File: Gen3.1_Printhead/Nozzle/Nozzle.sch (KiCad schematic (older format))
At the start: 74 parts, among them J1 IDC Conn

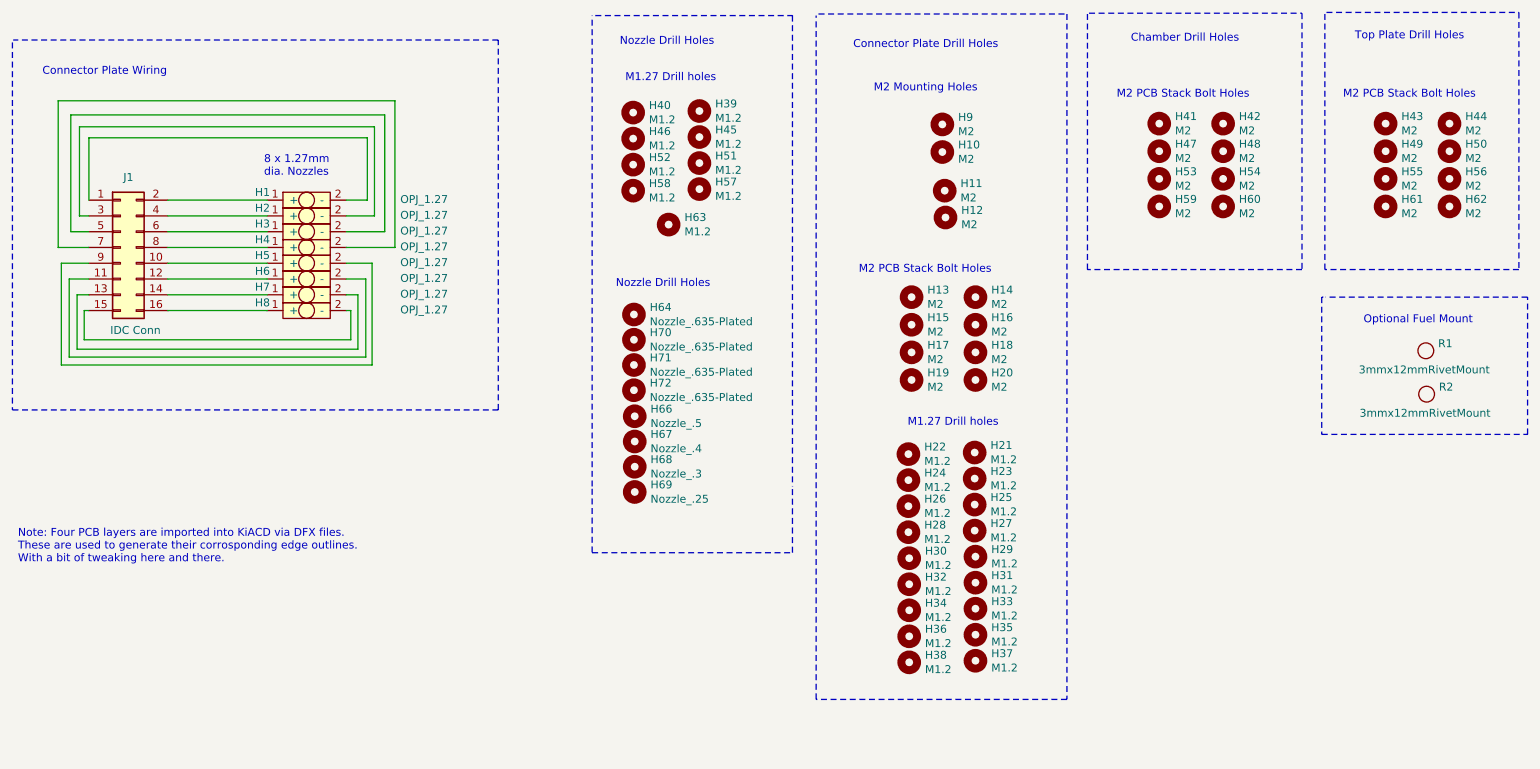
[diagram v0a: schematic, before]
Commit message: adding in Gen3.1a Conector PCB inlet modifications - hole reduced from 1.27mm to 1mm, or 0.8mm
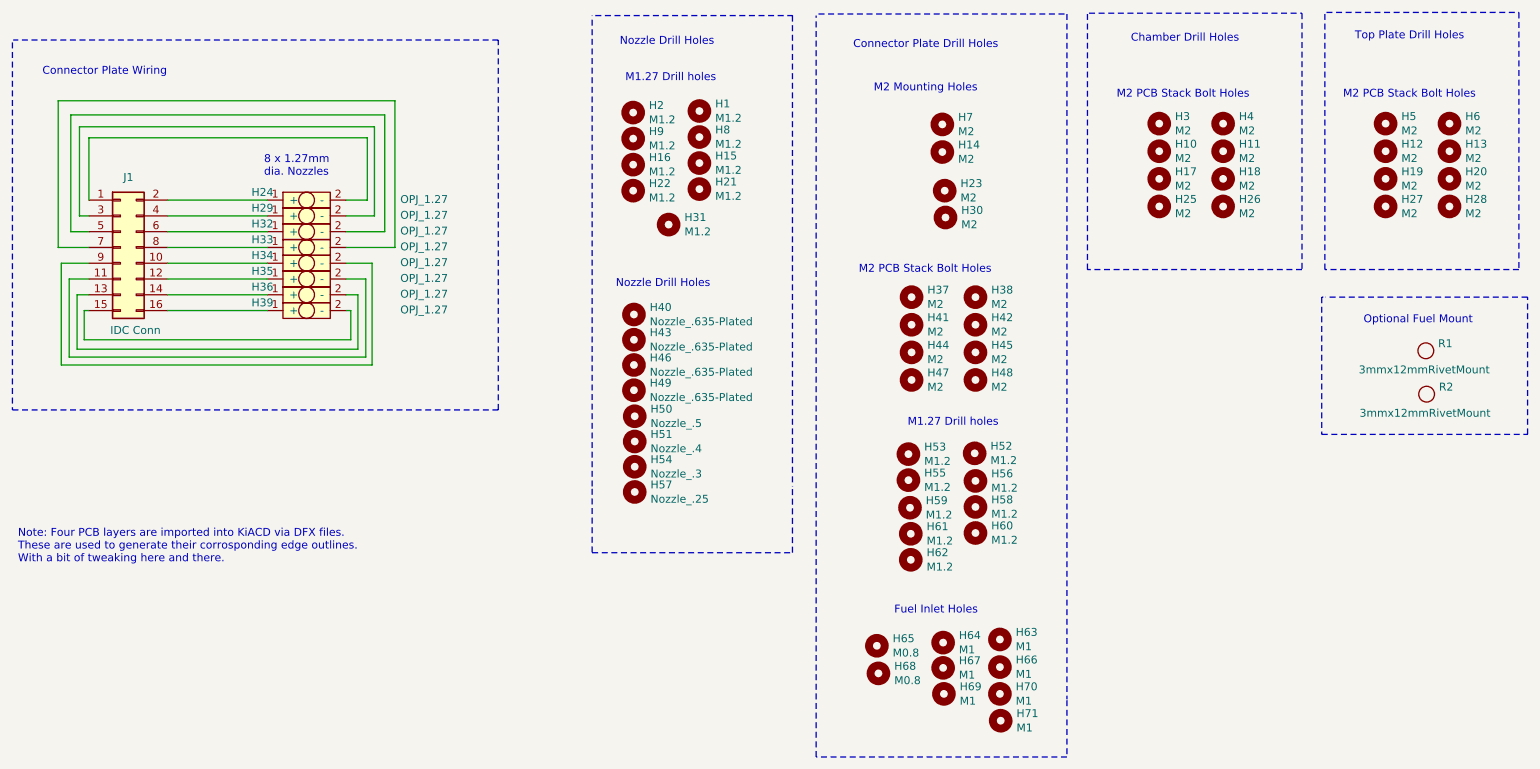
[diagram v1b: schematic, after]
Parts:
- H63: renamed from H29; value M1.2 -> M1; footprint Pauls_KiCAD_Libraries:MountingHole_1.2mm -> Pauls_KiCAD_Libraries:MountingHole_1mm
- H64: renamed from H31; value M1.2 -> M1; footprint Pauls_KiCAD_Libraries:MountingHole_1.2mm -> Pauls_KiCAD_Libraries:MountingHole_1mm
- H65: renamed from H38; value M1.2 -> M0.8; footprint Pauls_KiCAD_Libraries:MountingHole_1.2mm -> Pauls_KiCAD_Libraries:MountingHole_0.8mm
- H66: renamed from H25; value M1.2 -> M1; footprint Pauls_KiCAD_Libraries:MountingHole_1.2mm -> Pauls_KiCAD_Libraries:MountingHole_1mm
- H67: renamed from H34; value M1.2 -> M1; footprint Pauls_KiCAD_Libraries:MountingHole_1.2mm -> Pauls_KiCAD_Libraries:MountingHole_1mm
- H68: renamed from H36; value M1.2 -> M0.8; footprint Pauls_KiCAD_Libraries:MountingHole_1.2mm -> Pauls_KiCAD_Libraries:MountingHole_0.8mm
- H69: renamed from H26; value M1.2 -> M1; footprint Pauls_KiCAD_Libraries:MountingHole_1.2mm -> Pauls_KiCAD_Libraries:MountingHole_1mm
- H70: renamed from H27; value M1.2 -> M1; footprint Pauls_KiCAD_Libraries:MountingHole_1.2mm -> Pauls_KiCAD_Libraries:MountingHole_1mm
- H71: renamed from H21; value M1.2 -> M1; footprint Pauls_KiCAD_Libraries:MountingHole_1.2mm -> Pauls_KiCAD_Libraries:MountingHole_1mm
- renumbered H39 to H1, H47 to H10, H48 to H11, H49 to H12, H50 to H13, H10 to H14, H51 to H15, H52 to H16, H53 to H17, H54 to H18, H55 to H19, H40 to H2, H56 to H20, H57 to H21, H58 to H22, H11 to H23, H1 to H24, H59 to H25, H60 to H26, H61 to H27, H62 to H28, H2 to H29, H41 to H3, H12 to H30, H63 to H31, H3 to H32, H4 to H33, H5 to H34, H6 to H35, H7 to H36, H13 to H37, H14 to H38, H8 to H39, H42 to H4, H64 to H40, H15 to H41, H16 to H42, H70 to H43, H17 to H44, H18 to H45, H71 to H46, H19 to H47, H20 to H48, H72 to H49, H43 to H5, H66 to H50, H67 to H51, H23 to H52, H22 to H53, H68 to H54, H24 to H55, H33 to H56, H69 to H57, H35 to H58, H28 to H59, H44 to H6, H37 to H60, H30 to H61, H32 to H62, H9 to H7, H45 to H8, H46 to H9
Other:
- note added: "Fuel Inlet Holes"
- moved on the sheet: H52, H56, H58, H59, H60, H61, H62, H63, H64, H65, H66, H67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
